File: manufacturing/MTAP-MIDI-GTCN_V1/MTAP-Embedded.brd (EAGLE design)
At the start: 27.9 x 62.9 mm, 54 parts, among them IC1 ESP32-WROOM-32UE-N8, IC2 AMS1117-3.3, IC3 PCM1821IRTER, J1 629105150521

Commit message: New Layout
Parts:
- removed C10, C12: 1u, rcl_GruS:C0805
- removed C11, C13, C14: 10u, rcl_GruS:C0805
- removed C15, C17, C18, C20: 100n, rcl_GruS:C0805
- removed C16, C21: 10n, rcl_GruS:C0805
- removed C19: 680n, rcl_GruS:C0805
- removed IC3: PCM1821IRTER, adc-dac_GruS:WQFN20
- removed R12: 6k2, rcl_GruS:R0805
- removed R13: 2k4, rcl_GruS:R0805
- removed R14: 240, rcl_GruS:R0805
- removed R15: 5k1, rcl_GruS:R0805
- removed R16: 200, rcl_GruS:R0805
- removed R17: 750, rcl_GruS:R0805
- removed R3, R4: 0R, rcl_GruS:R0805
- removed V4: TLV9354IPWR, opv_GruS:SOP65P640X120-14N
- removed X2: (no value), con_GruS:MYLIB_SJ-SHORT
- added S3: (no value), switch_GruS:A68-A31
- moved R2 69.6 mm to (50.2, -14.0)
- moved C5 63.4 mm to (51.4, -7.62)
- moved C4 42.9 mm to (41.9, -14.0), turned to 0 degrees
- moved C3 33.7 mm to (41.9, -7.62), turned to 0 degrees
- moved S1 32.9 mm to (-19.1, 42.5)
- moved S2 32.9 mm to (-19.1, 42.5)
- moved C6 25.2 mm to (-12.7, 37.8)
- moved C7 24.9 mm to (-11.1, 45.1), turned to 90 degrees
- moved R11 17.2 mm to (35.6, 39.4)
- moved R10 10.2 mm to (2.54, 59.1), turned to 270 degrees
- moved R7 8.44 mm to (5.71, 60.0), turned to 0 degrees
- moved R1 8.31 mm to (23.8, 59.1), turned to 270 degrees
- moved R8 7.96 mm to (9.84, 60.0), turned to 180 degrees
- moved H1 6.97 mm to (25.7, 59.1), turned to 180 degrees
- moved D1 5.99 mm to (4.13, 53.7), turned to 180 degrees
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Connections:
- removed net AVDD: C12.1, C18.1, IC3.16, V4.4, X2.2
- removed net IN1P: C21.1, IC3.1, R17.2, V4.14
- removed net IN2M: IC3.4
- removed net IN2P: IC3.3
- removed net N$10: R14.1, R15.2, V4.1
- removed net N$11: C21.2, R16.2, V4.12
- removed net N$13: C11.1, C15.1, IC3.14
- removed net N$17: C13.1, C17.1, IC3.17
- removed net N$5: R12.1
- removed net N$6: C16.1, R12.2, V4.3
- removed net N$7: R13.2, R15.1, V4.2
- removed net N$8: C19.1, R14.2, R16.1, R17.1
- removed net N$9: C10.1, IC3.18
- new net RXD1: S3.6
- new net TXD1: S3.3
- net +3V3: no longer C14.1, C20.1, IC3.9, X2.1
- net BCLK: no longer IC3.7
- net FSYNC: no longer IC3.8
- net FTM0: no longer IC3.19
- net GND: no longer C10.2, C11.2, C12.2, C13.2, C14.2, C15.2, C16.2, C17.2, C18.2, C19.2, C20.2, IC3.10, IC3.15, IC3.2, IC3.20, IC3.21, IC3.22, IC3.23, IC3.24, IC3.25, IC3.5, R13.1, V4.10, V4.11, V4.13, V4.5, V4.6, V4.9
- net MD0: no longer IC3.12
- net MD1: no longer IC3.11
- net MSZ: no longer IC3.13
- net RXD: now also S3.2; no longer R3.2
- net RXD0: now also S3.4; no longer R4.1
- net SDATA: no longer IC3.6
- net TXD: now also S3.5; no longer R4.2
- net TXD0: now also S3.1; no longer R3.1
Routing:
- net GND: track 56.1 -> 0.00 mm, vias 34 -> 0
- net EN: track 52.9 -> 1.70 mm, vias 4 -> 0
- net +3V3: track 44.8 -> 8.28 mm, vias 9 -> 2
- net FTM0: track 36.4 -> 0.00 mm, vias 2 -> 0
- net RXD0: track 29.2 -> 0.00 mm, vias 2 -> 0
- net MSZ: track 27.7 -> 0.00 mm, vias 2 -> 0
- net TXD0: track 27.1 -> 0.00 mm, vias 2 -> 0
- net GPIO0: track 27.9 -> 1.70 mm, vias 1 -> 0
- net MD0: track 23.3 -> 0.00 mm, vias 2 -> 0
- net MD1: track 19.3 -> 0.00 mm, vias 2 -> 0
- net SDATA: track 17.2 -> 0.00 mm, vias 2 -> 0
- net BCLK: track 14.1 -> 0.00 mm, vias 2 -> 0
- net FSYNC: track 12.3 -> 0.00 mm, vias 2 -> 0
- net DTR: track 17.2 -> 6.55 mm, vias 2 -> 0
- net TXD: track 9.76 -> 0.00 mm
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- removed copper zone on layer 1, net +3V3
- removed copper zone on layer 16, net +3V3
- removed copper zone on layer 1, net AVDD
- removed copper zone on layer 1, net GND
- removed copper zone on layer 16, net GND
- removed copper zone on layer 1, net PGND
- removed copper zone on layer 16, net PGND

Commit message: upd board
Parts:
- removed S3: (no value), switch_GruS:A68-A31
- added S4: (no value), switch_GruS:452404020202
- moved R2 47.1 mm to (21.3, 23.2), turned to 270 degrees
- moved C5 44.7 mm to (19.1, 23.2), turned to 90 degrees
- moved C4 40.2 mm to (19.1, 19.1), turned to 270 degrees
- moved C3 33.7 mm to (21.3, 19.1), turned to 270 degrees
- moved S1 32.1 mm to (8.89, 58.4), flipped to the top
- moved S2 25.8 mm to (1.27, 58.4)
- moved R11 22.2 mm to (13.3, 39.1)
- moved C6 19.4 mm to (-0.32, 52.7), flipped to the top
- moved H1 15.6 mm to (13.7, 49.2)
- moved C7 14.6 mm to (-0.32, 54.9), flipped to the top, turned to 0 degrees
- moved R1 11.3 mm to (16.8, 50.2), turned to 0 degrees
- moved C1 10.7 mm to (21.6, 41.6), turned to 270 degrees
- moved D3 8.90 mm to (10.8, 47.6), turned to 0 degrees
- moved R6 8.84 mm to (-0.32, 40.3), turned to 180 degrees
- moved V2 8.55 mm to (-0.32, 49.8), turned to 90 degrees
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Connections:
- removed net GPIO26: IC1.11
- removed net GPIO27: IC1.12
- net EN: now also S2.1, S2.2; no longer S2.3, S2.4
- net PGND: now also S2.3, S2.4; no longer S2.1, S2.2
- net RXD: now also S4.2; no longer S3.2
- net RXD0: now also S4.4; no longer S3.4
- net RXD1: now also IC1.12, S4.6; no longer S3.6
- net TXD: now also S4.5; no longer S3.5
- net TXD0: now also S4.1; no longer S3.1
- net TXD1: now also IC1.11, S4.3; no longer S3.3
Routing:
- net EN: track 1.70 -> 61.4 mm, vias 0 -> 5
- net GPIO0: track 1.70 -> 35.2 mm, vias 0 -> 2
- net GND: track 0.00 -> 29.6 mm, vias 0 -> 12
- net +3V3: track 8.28 -> 36.1 mm
- net RXD0: track 0.00 -> 21.8 mm, vias 0 -> 1
- net TXD0: track 0.00 -> 19.8 mm, vias 0 -> 1
- net RXD1: track 0.00 -> 13.2 mm, vias 0 -> 1
- net VBUS: track 6.38 -> 18.0 mm
- net TXD1: track 0.00 -> 11.2 mm, vias 0 -> 1
- net USB_DN: track 11.5 -> 19.1 mm, vias 0 -> 2
- net RXD: track 0.00 -> 6.76 mm
- net DTR: track 6.55 -> 10.8 mm, vias 0 -> 2
- net TXD: track 0.00 -> 3.25 mm
- net RTS: track 5.52 -> 8.33 mm
- net +5V: track 5.09 -> 7.84 mm
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- added copper zone on layer 1, net +3V3
- added copper zone on layer 16, net AGND
- added copper zone on layer 1, net GND
- added copper zone on layer 16, net GND
- added copper zone on layer 1, net PGND
- added copper zone on layer 16, net PGND
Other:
- board size 27.9 x 62.9 mm -> 30.5 x 45.1 mm

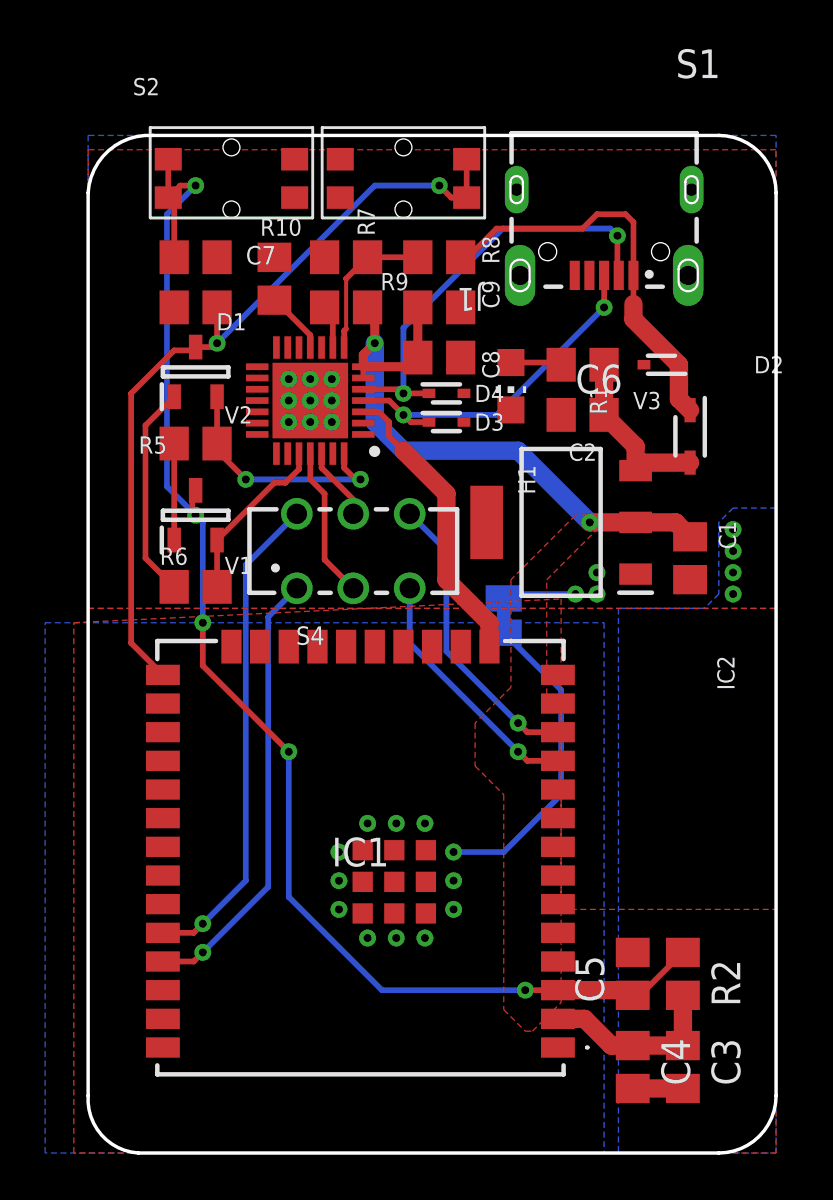
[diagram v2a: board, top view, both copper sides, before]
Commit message: Upd PCB
Finished new Board essentials
Analog parts excluded and yet to be implemented
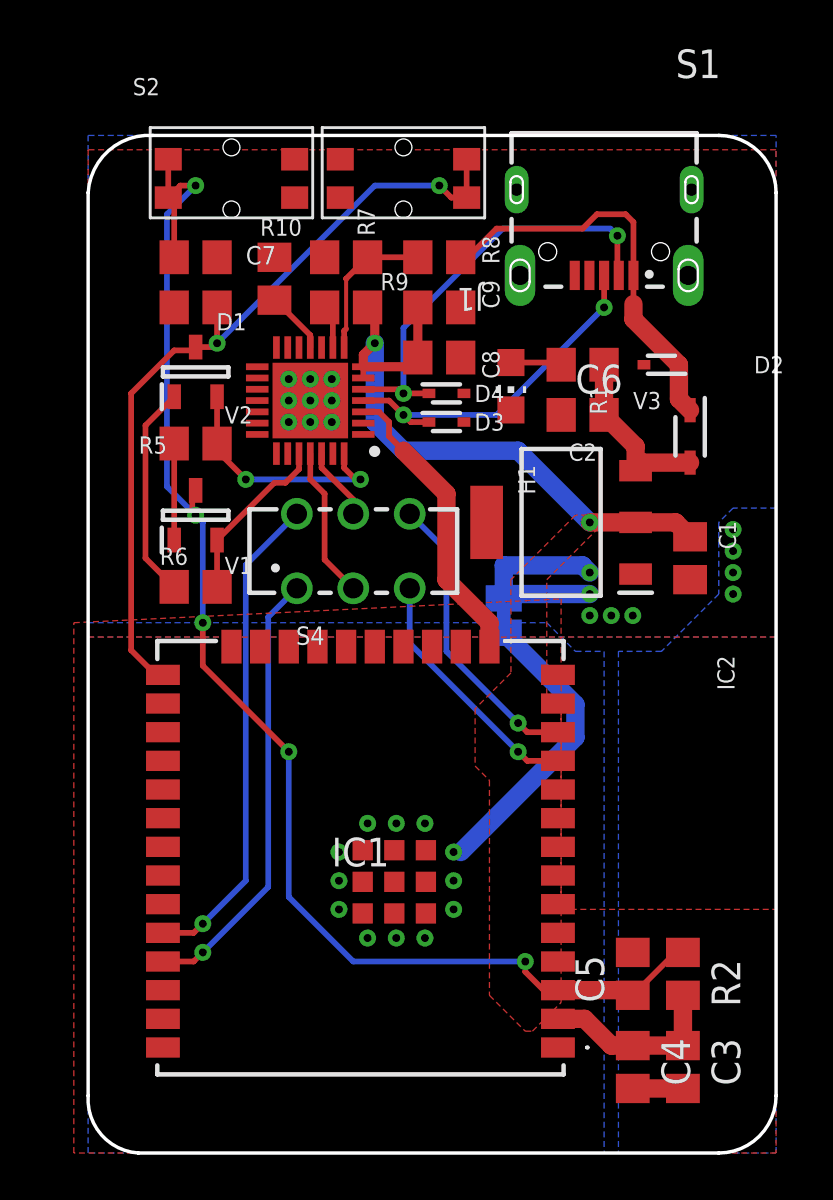
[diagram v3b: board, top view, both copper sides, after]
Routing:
- net PGND: track 3.25 -> 9.29 mm, vias 12 -> 14
- net GND: track 29.6 -> 29.0 mm
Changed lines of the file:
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@@
 <wire x1="12.7" y1="38.735" x2="10.795" y2="40.64" width="0.8128" layer="1"/>
 <polygon width="0.254" layer="16" isolate="0.4064">
-<vertex x="-6.985" y="38.735"/>
-<vertex x="17.78" y="38.735"/>
+<vertex x="-5.08" y="38.735"/>
+<vertex x="15.24" y="38.735"/>
+<vertex x="16.51" y="37.465"/>
+<vertex x="17.78" y="37.465"/>
 <vertex x="17.78" y="15.24"/>
-<vertex x="-6.985" y="15.24"/>
+<vertex x="-5.08" y="15.24"/>
 </polygon>
 <via x="9.8425" y="29.845" extent="1-16" drill="0.35"/>
@@
 <via x="11.1125" y="27.305" extent="1-16" drill="0.35"/>
 <via x="11.1125" y="26.035" extent="1-16" drill="0.35"/>
-<wire x1="13.335" y1="38.2905" x2="15.875" y2="35.7505" width="0.254" layer="16"/>
-<wire x1="15.875" y1="31.115" x2="13.335" y2="28.575" width="0.254" layer="16"/>
-<wire x1="13.335" y1="28.575" x2="11.1125" y2="28.575" width="0.254" layer="16"/>
-<wire x1="15.875" y1="35.7505" x2="15.875" y2="31.115" width="0.254" layer="16"/>
+<wire x1="11.43" y1="28.575" x2="11.1125" y2="28.575" width="0.254" layer="16"/>
+<wire x1="13.335" y1="38.2905" x2="16.51" y2="35.1155" width="0.8128" layer="16"/>
+<wire x1="16.51" y1="33.655" x2="11.43" y2="28.575" width="0.8128" layer="16"/>
+<wire x1="16.51" y1="35.1155" x2="16.51" y2="33.655" width="0.8128" layer="16"/>
 </signal>
 <signal name="N$1">
@@
 <wire x1="-0.465" y1="50.8" x2="-1.27" y2="50.8" width="0.254" layer="1"/>
 <wire x1="-1.27" y1="50.8" x2="-3.175" y2="48.895" width="0.254" layer="1"/>
-<wire x1="-3.175" y1="37.835" x2="-1.765" y2="36.425" width="0.254" layer="1"/>
-<wire x1="-3.175" y1="48.895" x2="-3.175" y2="37.835" width="0.254" layer="1"/>
+<wire x1="-2.0825" y1="36.425" x2="-1.765" y2="36.425" width="0.254" layer="1"/>
+<wire x1="-2.0825" y1="36.425" x2="-3.175" y2="37.5175" width="0.254" layer="1"/>
+<wire x1="-3.175" y1="48.895" x2="-3.175" y2="37.5175" width="0.254" layer="1"/>
 </signal>
 <signal name="USB_DP">
@@
 <wire x1="0" y1="43.18" x2="0" y2="38.735" width="0.254" layer="16"/>
 <via x="0" y="38.735" extent="1-16" drill="0.35"/>
-<wire x1="15.735" y1="22.455" x2="14.2875" y2="22.455" width="0.254" layer="1"/>
-<via x="14.2875" y="22.455" extent="1-16" drill="0.35"/>
+<wire x1="15.735" y1="22.455" x2="15.1" y2="22.455" width="0.254" layer="1"/>
+<wire x1="15.1" y1="22.455" x2="14.2875" y2="23.2675" width="0.254" layer="1"/>
+<wire x1="14.2875" y1="23.725" x2="14.2875" y2="23.2675" width="0.254" layer="1"/>
+<via x="14.2875" y="23.725" extent="1-16" drill="0.35"/>
 <wire x1="0" y1="38.735" x2="0" y2="36.83" width="0.254" layer="1"/>
 <wire x1="0" y1="36.83" x2="3.81" y2="33.02" width="0.254" layer="1"/>
 <via x="3.81" y="33.02" extent="1-16" drill="0.35"/>
 <wire x1="3.81" y1="33.02" x2="3.81" y2="26.5825" width="0.254" layer="16"/>
-<wire x1="7.9375" y1="22.455" x2="3.81" y2="26.5825" width="0.254" layer="16"/>
-<wire x1="7.9375" y1="22.455" x2="14.2875" y2="22.455" width="0.254" layer="16"/>
-<wire x1="15.735" y1="22.455" x2="18.8225" y2="22.455" width="0.8128" layer="1"/>
-<wire x1="18.8225" y1="22.455" x2="19.05" y2="22.2275" width="0.8128" layer="1"/>
-<wire x1="19.05" y1="22.2275" x2="19.3725" y2="22.2275" width="0.254" layer="1"/>
-<wire x1="19.3725" y1="22.2275" x2="21.2725" y2="24.1275" width="0.254" layer="1"/>
+<wire x1="6.6675" y1="23.725" x2="3.81" y2="26.5825" width="0.254" layer="16"/>
+<wire x1="6.6675" y1="23.725" x2="14.2875" y2="23.725" width="0.254" layer="16"/>
+<wire x1="19.05" y1="22.2275" x2="20.95" y2="24.1275" width="0.254" layer="1"/>
+<wire x1="20.95" y1="24.1275" x2="21.2725" y2="24.1275" width="0.254" layer="1"/>
+<wire x1="19.05" y1="22.2275" x2="18.8225" y2="22.455" width="0.8128" layer="1"/>
+<wire x1="18.8225" y1="22.455" x2="15.735" y2="22.455" width="0.8128" layer="1"/>
 </signal>
 <signal name="DCD">
@@
 <vertex x="16.51" y="43.4975"/>
 <vertex x="13.6525" y="40.64"/>
-<vertex x="13.6525" y="35.8775"/>
-<vertex x="12.065" y="34.29"/>
+<vertex x="13.6525" y="36.5125"/>
+<vertex x="12.065" y="34.925"/>
 <vertex x="12.065" y="32.385"/>
-<vertex x="13.335" y="31.115"/>
-<vertex x="13.335" y="21.59"/>
+<vertex x="12.7" y="31.75"/>
+<vertex x="12.7" y="22.225"/>
 </polygon>
 <wire x1="21.2725" y1="20" x2="19.05" y2="20" width="0.8128" layer="1"/>
-<wire x1="21.2725" y1="22.2275" x2="21.2725" y2="20" width="0.8128" layer="1"/>
 <wire x1="15.735" y1="21.185" x2="16.915" y2="21.185" width="0.8128" layer="1"/>
 <wire x1="18.1" y1="20" x2="19.05" y2="20" width="0.8128" layer="1"/>
 <wire x1="16.915" y1="21.185" x2="18.1" y2="20" width="0.8128" layer="1"/>
+<wire x1="21.2725" y1="22.2275" x2="21.2725" y2="20" width="0.8128" layer="1"/>
 </signal>
 <signal name="PGND">
@@
 <polygon width="0.254" layer="1" rank="4">
 <vertex x="-5.08" y="59.69"/>
-<vertex x="-5.08" y="39.37"/>
-<vertex x="25.4" y="39.37"/>
+<vertex x="-5.08" y="38.1"/>
+<vertex x="25.4" y="38.1"/>
 <vertex x="25.4" y="59.69"/>
 </polygon>
@@
 <contactref element="S2" pad="3"/>
 <polygon width="0.254" layer="16" isolate="0.4064" rank="4">
-<vertex x="-5.08" y="39.37"/>
-<vertex x="25.4" y="39.37"/>
+<vertex x="-5.08" y="38.1"/>
+<vertex x="25.4" y="38.1"/>
 <vertex x="25.4" y="60.325"/>
 <vertex x="-5.08" y="60.325"/>
 </polygon>
-<via x="17.4625" y="40.9575" extent="1-16" drill="0.35"/>
-<via x="17.4625" y="40.005" extent="1-16" drill="0.35"/>
-<via x="16.51" y="40.005" extent="1-16" drill="0.35"/>
-<wire x1="13.335" y1="39.8145" x2="13.5255" y2="40.005" width="0.254" layer="16"/>
-<wire x1="13.5255" y1="40.005" x2="16.51" y2="40.005" width="0.254" layer="16"/>
+<via x="18.0975" y="39.0525" extent="1-16" drill="0.35"/>
+<via x="17.145" y="39.0525" extent="1-16" drill="0.35"/>
+<via x="19.05" y="39.0525" extent="1-16" drill="0.35"/>
+<via x="17.145" y="40.005" extent="1-16" drill="0.35"/>
+<via x="17.145" y="40.9575" extent="1-16" drill="0.35"/>
+<wire x1="13.335" y1="39.8145" x2="13.5255" y2="40.005" width="0.8128" layer="16"/>
+<wire x1="13.5255" y1="40.005" x2="17.145" y2="40.005" width="0.8128" layer="16"/>
+<wire x1="13.335" y1="39.8145" x2="13.335" y2="41.275" width="0.8128" layer="16"/>
+<wire x1="13.335" y1="41.275" x2="16.8275" y2="41.275" width="0.8128" layer="16"/>
+<wire x1="16.8275" y1="41.275" x2="17.145" y2="40.9575" width="0.8128" layer="16"/>
 <wire x1="21.505" y1="54.123" x2="21.655" y2="57.923" width="0" layer="19" extent="1-1"/>
 <wire x1="19.545" y1="50.165" x2="21.505" y2="54.123" width="0" layer="19" extent="1-1"/>
@@
 <via x="23.495" y="41.91" extent="1-16" drill="0.35"/>
 <via x="23.495" y="42.8625" extent="1-16" drill="0.35"/>
-<polygon width="0.254" layer="16" pour="cutout" isolate="0.4064">
-<vertex x="18.415" y="39.37"/>
+<polygon width="0.254" layer="16" isolate="0.4064">
+<vertex x="18.415" y="37.465"/>
 <vertex x="18.415" y="15.24"/>
 <vertex x="25.4" y="15.24"/>
@@
 <vertex x="22.86" y="43.18"/>
 <vertex x="22.86" y="40.005"/>
-<vertex x="22.225" y="39.37"/>
-</polygon>
-<wire x1="23.495" y1="41.91" x2="23.495" y2="40.9575" width="0" layer="19" extent="1-1"/>
-<wire x1="23.495" y1="42.8625" x2="23.495" y2="41.91" width="0" layer="19" extent="1-1"/>
-<wire x1="23.495" y1="40.005" x2="23.495" y2="40.9575" width="0" layer="19" extent="1-1"/>
+<vertex x="20.32" y="37.465"/>
+</polygon>
 </signal>
 </signals>

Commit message: adp adc #3 pcb
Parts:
- added D5: MCP33131-05-E, adc-dac_GruS:MSOP10
- added N1: TC2015, vreg_GruS:SOT-23-5
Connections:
- new net +1V8: D5.2, N1.5
- new net ADI: D5.9
- new net AGND: D5.4, D5.5, N1.4
- new net N$10: N1.2
- new net N$11: D5.3
- new net N$6: D5.7
- new net N$7: D5.8
- new net N$8: N1.3
- new net N$9: D5.1
- net +3V3: now also N1.1
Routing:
- net GND: track 29.0 -> 29.8 mm
